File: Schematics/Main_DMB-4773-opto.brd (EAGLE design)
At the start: 102.8 x 86.9 mm, 133 parts

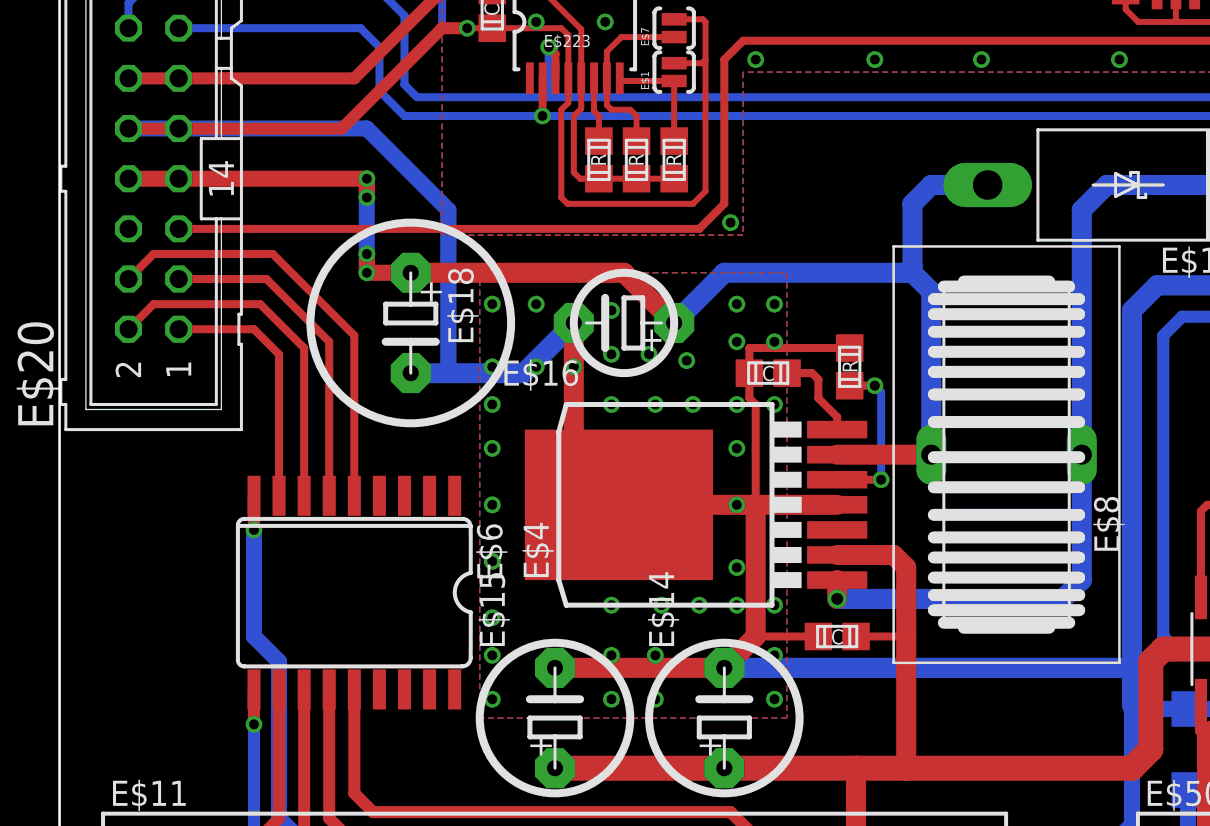
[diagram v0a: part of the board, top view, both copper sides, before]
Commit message: Ajout cape et modification cartes C
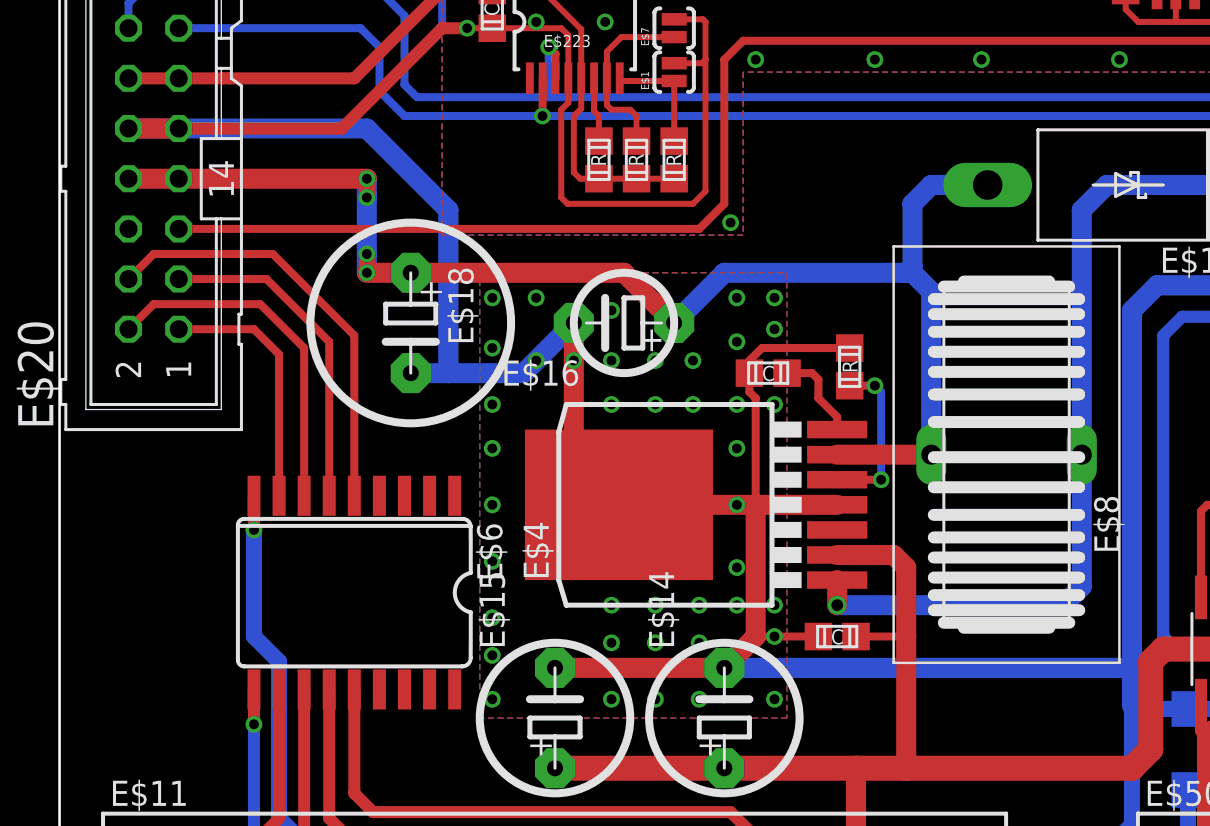
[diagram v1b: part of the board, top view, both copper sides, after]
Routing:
- net S$82: track 43.5 -> 44.1 mm
- net GND: track 831.5 -> 831.1 mm, vias 83 -> 85
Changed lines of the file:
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@@
 <wire x1="11.1125" y1="17.4625" x2="11.1125" y2="9.525" width="0.8128" layer="16"/>
 <wire x1="11.1125" y1="9.525" x2="12.3825" y2="8.255" width="0.8128" layer="16"/>
-<wire x1="6.0325" y1="44.45" x2="15.5575" y2="44.45" width="0.8128" layer="16"/>
-<wire x1="15.5575" y1="44.45" x2="19.685" y2="40.3225" width="0.8128" layer="16"/>
-<wire x1="19.685" y1="40.3225" x2="19.685" y2="32.0675" width="0.8128" layer="16"/>
+<wire x1="6.0325" y1="44.45" x2="15.5575" y2="44.45" width="1.016" layer="16"/>
+<wire x1="15.5575" y1="44.45" x2="19.685" y2="40.3225" width="1.016" layer="16"/>
+<wire x1="19.685" y1="40.3225" x2="19.685" y2="32.0675" width="1.016" layer="16"/>
 <contactref element="E$20" pad="10"/>
 <contactref element="E$20" pad="9"/>
-<wire x1="3.4925" y1="44.45" x2="6.0325" y2="44.45" width="0.6096" layer="1"/>
-<wire x1="3.4925" y1="44.45" x2="6.0325" y2="44.45" width="0.8128" layer="16"/>
+<wire x1="3.4925" y1="44.45" x2="6.0325" y2="44.45" width="1.016" layer="1"/>
+<wire x1="3.4925" y1="44.45" x2="6.0325" y2="44.45" width="1.016" layer="16"/>
 <polygon width="0.254" layer="1" spacing="0.254" isolate="0.254">
 <vertex x="0" y="83.185"/>
@@
 <wire x1="99.06" y1="53.34" x2="99.06" y2="48.26" width="0.4064" layer="1"/>
 <contactref element="E$12" pad="2"/>
-<wire x1="40.005" y1="33.3375" x2="34.925" y2="33.3375" width="0.4064" layer="1"/>
+<wire x1="40.005" y1="33.3375" x2="35.56" y2="33.3375" width="0.4064" layer="1"/>
 <contactref element="E$5" pad="1"/>
-<wire x1="34.925" y1="33.3375" x2="34.925" y2="32.0674" width="0.4064" layer="1"/>
-<wire x1="34.925" y1="32.0674" x2="34.925" y2="30.7975" width="0.4064" layer="1"/>
-<wire x1="34.925" y1="30.7975" x2="35.2425" y2="30.48" width="0.4064" layer="1"/>
-<wire x1="35.2425" y1="30.48" x2="35.2425" y2="25.4" width="0.4064" layer="1"/>
+<wire x1="35.56" y1="33.3375" x2="34.925" y2="32.7025" width="0.4064" layer="1"/>
+<wire x1="34.925" y1="32.7025" x2="34.925" y2="32.0674" width="0.4064" layer="1"/>
+<wire x1="34.925" y1="32.0674" x2="34.925" y2="31.115" width="0.4064" layer="1"/>
+<wire x1="34.925" y1="31.115" x2="35.2425" y2="30.7975" width="0.4064" layer="1"/>
+<wire x1="35.2425" y1="30.7975" x2="35.2425" y2="25.4" width="0.4064" layer="1"/>
 <polygon width="0.254" layer="1" spacing="0.254" isolate="0.254">
 <vertex x="33.655" y="14.605"/>
@@
 <via x="34.29" y="20.32" extent="1-16" drill="0.5"/>
 <via x="32.385" y="20.32" extent="1-16" drill="0.5"/>
-<via x="30.48" y="20.32" extent="1-16" drill="0.5"/>
+<via x="30.1625" y="20.32" extent="1-16" drill="0.5"/>
 <via x="27.94" y="20.32" extent="1-16" drill="0.5"/>
 <via x="27.94" y="30.48" extent="1-16" drill="0.5"/>
-<via x="29.845" y="33.02" extent="1-16" drill="0.5"/>
+<via x="30.1625" y="32.7025" extent="1-16" drill="0.5"/>
 <via x="30.1625" y="30.48" extent="1-16" drill="0.5"/>
 <via x="32.0675" y="30.48" extent="1-16" drill="0.5"/>
-<via x="31.75" y="32.7025" extent="1-16" drill="0.5"/>
-<via x="27.94" y="17.78" extent="1-16" drill="0.5"/>
+<via x="32.0675" y="32.7025" extent="1-16" drill="0.5"/>
+<via x="27.94" y="18.415" extent="1-16" drill="0.5"/>
 <via x="30.1625" y="15.5575" extent="1-16" drill="0.5"/>
-<via x="30.1625" y="17.78" extent="1-16" drill="0.5"/>
+<via x="30.1625" y="18.415" extent="1-16" drill="0.5"/>
 <via x="27.94" y="15.5575" extent="1-16" drill="0.5"/>
 <via x="21.9075" y="19.685" extent="1-16" drill="0.5"/>
 <via x="21.9075" y="17.78" extent="1-16" drill="0.5"/>
 <via x="21.9075" y="15.5575" extent="1-16" drill="0.5"/>
-<via x="27.94" y="33.02" extent="1-16" drill="0.5"/>
+<via x="27.94" y="32.7025" extent="1-16" drill="0.5"/>
 <via x="27.94" y="35.2425" extent="1-16" drill="0.5"/>
 <via x="34.29" y="33.655" extent="1-16" drill="0.5"/>
-<via x="34.29" y="35.56" extent="1-16" drill="0.5"/>
-<via x="36.195" y="35.56" extent="1-16" drill="0.5"/>
-<via x="36.195" y="33.655" extent="1-16" drill="0.5"/>
-<via x="26.035" y="32.385" extent="1-16" drill="0.5"/>
-<via x="24.13" y="32.385" extent="1-16" drill="0.5"/>
-<via x="21.9075" y="32.385" extent="1-16" drill="0.5"/>
+<via x="34.29" y="35.8775" extent="1-16" drill="0.5"/>
+<via x="36.195" y="35.8775" extent="1-16" drill="0.5"/>
+<via x="36.195" y="34.29" extent="1-16" drill="0.5"/>
+<via x="26.035" y="32.7025" extent="1-16" drill="0.5"/>
+<via x="24.13" y="32.7025" extent="1-16" drill="0.5"/>
+<via x="21.9075" y="33.3375" extent="1-16" drill="0.5"/>
 <via x="36.195" y="15.5575" extent="1-16" drill="0.5"/>
 <via x="36.195" y="20.32" extent="1-16" drill="0.5"/>
-<via x="36.195" y="17.78" extent="1-16" drill="0.5"/>
+<via x="36.195" y="18.7325" extent="1-16" drill="0.5"/>
 <via x="21.9075" y="25.4" extent="1-16" drill="0.5"/>
 <via x="21.9075" y="22.5425" extent="1-16" drill="0.5"/>
 <via x="21.9075" y="28.2575" extent="1-16" drill="0.5"/>
 <via x="21.9075" y="30.48" extent="1-16" drill="0.5"/>
-<via x="21.9075" y="35.56" extent="1-16" drill="0.5"/>
-<via x="24.13" y="35.56" extent="1-16" drill="0.5"/>
+<via x="21.9075" y="35.8775" extent="1-16" drill="0.5"/>
+<via x="24.13" y="35.8775" extent="1-16" drill="0.5"/>
 <via x="36.195" y="30.48" extent="1-16" drill="0.5"/>
+<via x="32.385" y="15.5575" extent="1-16" drill="0.5"/>
+<via x="32.385" y="18.415" extent="1-16" drill="0.5"/>
 </signal>
 <signal name="VCC">
@@
 <contactref element="E$4" pad="1"/>
 <contactref element="E$8" pad="1"/>
-<wire x1="39.37" y1="21.59" x2="39.37" y2="20.6375" width="1.016" layer="1"/>
-<via x="39.37" y="20.6375" extent="1-16" drill="0.6"/>
-<wire x1="39.37" y1="20.6375" x2="50.8" y2="20.6375" width="1.016" layer="16"/>
-<wire x1="50.8" y1="20.6375" x2="51.7525" y2="21.59" width="1.016" layer="16"/>
-<wire x1="51.7525" y1="21.59" x2="51.7525" y2="27.94" width="1.016" layer="16"/>
+<wire x1="39.37" y1="21.59" x2="39.37" y2="20.32" width="1.016" layer="1"/>
+<via x="39.37" y="20.32" extent="1-16" drill="0.6"/>
+<wire x1="39.37" y1="20.32" x2="50.8" y2="20.32" width="1.016" layer="16"/>
+<wire x1="50.8" y1="20.32" x2="51.7525" y2="21.2725" width="1.016" layer="16"/>
+<wire x1="51.7525" y1="21.2725" x2="51.7525" y2="27.94" width="1.016" layer="16"/>
 <contactref element="E$17" pad="C"/>
 <wire x1="51.7525" y1="27.94" x2="51.7525" y2="40.3225" width="1.016" layer="16"/>
@@
 <contactref element="E$20" pad="8"/>
 <contactref element="E$20" pad="7"/>
-<wire x1="3.4925" y1="41.91" x2="6.0325" y2="41.91" width="0.8128" layer="1"/>
+<wire x1="3.4925" y1="41.91" x2="6.0325" y2="41.91" width="1.016" layer="1"/>
 <contactref element="E$4" pad="6"/>
 <contactref element="E$8" pad="2"/>
@@
 <wire x1="17.78" y1="37.1475" x2="28.575" y2="37.1475" width="1.016" layer="1"/>
 <wire x1="28.575" y1="37.1475" x2="31.115" y2="34.6075" width="1.016" layer="1"/>
-<wire x1="17.78" y1="37.1475" x2="15.5575" y2="37.1475" width="0.8128" layer="1"/>
+<wire x1="17.78" y1="37.1475" x2="15.5575" y2="37.1475" width="1.016" layer="1"/>
 <wire x1="15.5575" y1="37.1475" x2="15.5575" y2="38.1" width="0.8128" layer="1"/>
 <wire x1="15.5575" y1="40.9575" x2="15.5575" y2="41.91" width="0.8128" layer="1"/>
-<wire x1="15.5575" y1="41.91" x2="6.0325" y2="41.91" width="0.8128" layer="1"/>
+<wire x1="15.5575" y1="41.91" x2="6.0325" y2="41.91" width="1.016" layer="1"/>
 <via x="15.5575" y="40.9575" extent="1-16" drill="0.5"/>
 <via x="15.5575" y="41.91" extent="1-16" drill="0.5"/>
 <via x="15.5575" y="38.1" extent="1-16" drill="0.5"/>
 <via x="15.5575" y="37.1475" extent="1-16" drill="0.5"/>
-<wire x1="15.5575" y1="41.91" x2="15.5575" y2="40.9575" width="0.8128" layer="16"/>
-<wire x1="15.5575" y1="40.9575" x2="15.5575" y2="38.1" width="0.8128" layer="16"/>
-<wire x1="15.5575" y1="38.1" x2="15.5575" y2="37.1475" width="0.8128" layer="16"/>
+<wire x1="15.5575" y1="41.91" x2="15.5575" y2="40.9575" width="1.016" layer="16"/>
+<wire x1="15.5575" y1="40.9575" x2="15.5575" y2="38.1" width="1.016" layer="16"/>
+<wire x1="15.5575" y1="38.1" x2="15.5575" y2="37.1475" width="1.016" layer="16"/>
 </signal>
 <signal name="S$35">
